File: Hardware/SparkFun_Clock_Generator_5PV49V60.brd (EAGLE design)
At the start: 27.9 x 25.4 mm, 75 parts, among them J1 QWIIC_RIGHT_ANGLE, J2 QWIIC_RIGHT_ANGLE, U1 IDT_5P49V60_CLOCK_GENERATOR, Y1 16MHz

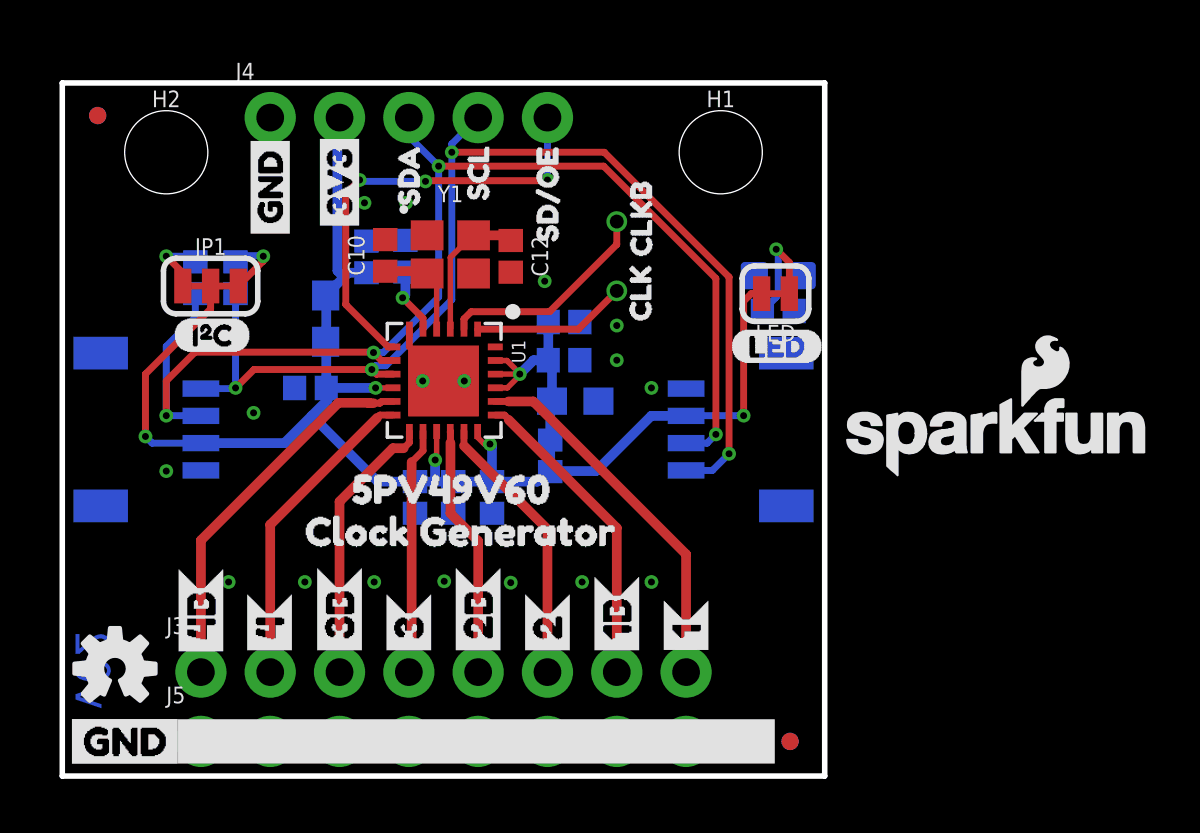
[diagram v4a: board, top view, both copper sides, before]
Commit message: Updates board with select jumper to enable select mode and fixes labels
* Also swaps clock out 4 and 4B
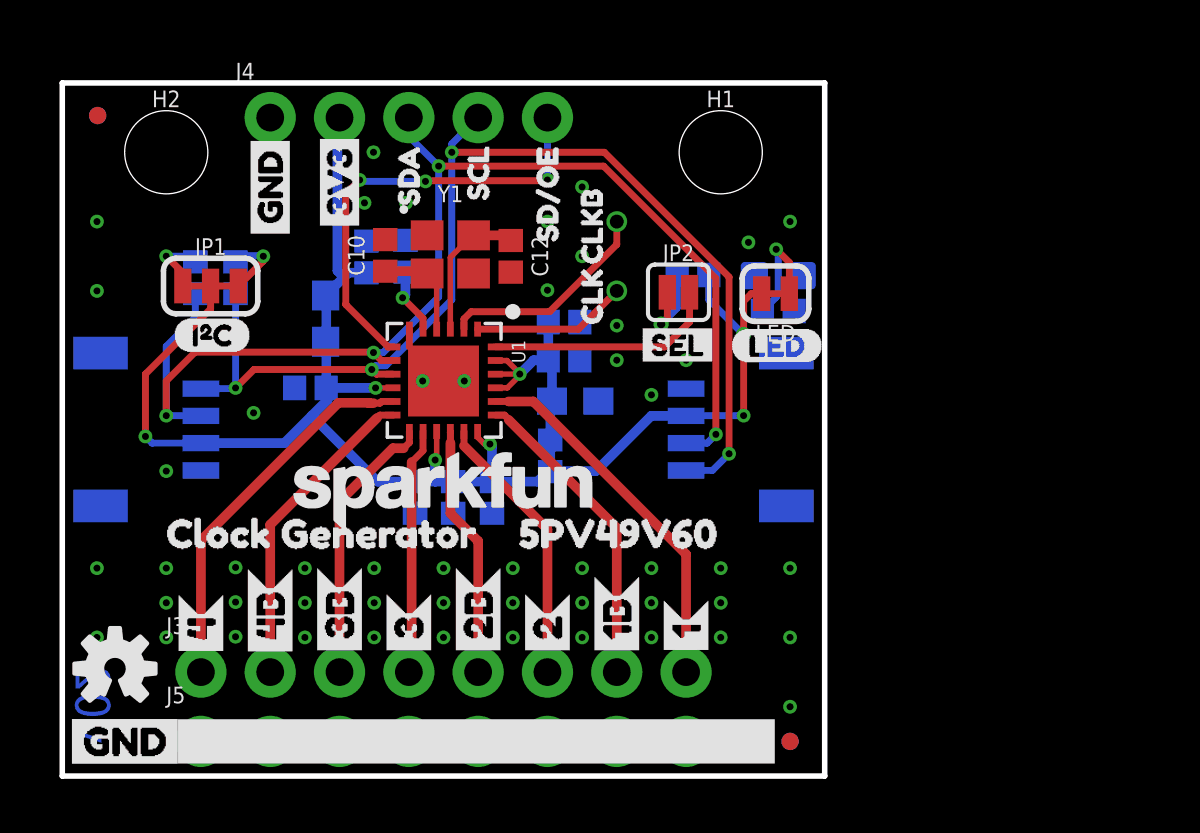
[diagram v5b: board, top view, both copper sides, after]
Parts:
- added JP2: JUMPER-SMT_2_NO_SILK, SparkFun-Jumpers:SMT-JUMPER_2_NO_SILK
- added R5: 10k, SparkFun-Resistors:0402
- added U$1: (no value), select:SEL0
- LOGO1: value SFE_LOGO_NAME_FLAME.1_INCH -> SFE_LOGO_NAME.1_INCH; device SparkFun-Aesthetics:SFE_LOGO_NAME_FLAME_.1 -> SparkFun-Aesthetics:SFE_LOGO_NAME_.1
- U$31: device Even more labels:CLKB13 -> Even more labels:CLK12
- U$32: device Even more labels:CLK11 -> Even more labels:CLKB13
- moved LOGO1 20.4 mm to (14.0, 10.4)
- moved U$31 6.38 mm to (21.4, 16.0), turned to 90 degrees
- moved U$17 6.33 mm to (15.8, 8.89)
- moved U$16 5.08 mm to (2.92, 8.89)
- moved U$4 3.48 mm to (27.8, 19.8)
- moved U$15 2.54 mm to (5.08, 9.42)
- moved U$25 2.54 mm to (7.62, 4.09)
- moved U$11 2.51 mm to (7.59, 10.4)
- moved U$38 2.51 mm to (5.08, 4.06)
- moved U$34 1.82 mm to (19.4, 18.1)
- moved U$33 1.78 mm to (19.4, 15.9)
- moved U$32 1.24 mm to (21.4, 18.3), turned to 90 degrees
- moved LOGO3 0.18 mm to (25.8, 8.38)
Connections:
- new net N$7: JP2.1, R5.2
- net 3.3V: now also R5.1
- net OUT4: now also J3.1, U1.P11; no longer J3.2, U1.P12
- net OUT4B: now also J3.2, U1.P12; no longer J3.1, U1.P11
- net SEL_I2CB: now also JP2.2
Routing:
- net SEL_I2CB: track 0.00 -> 8.59 mm
- net N$7: track 0.00 -> 3.31 mm, vias 0 -> 1
- net 3.3V: track 69.1 -> 71.8 mm, vias 7 -> 8
- net OUT4B: track 14.0 -> 11.6 mm
- net OUT4: track 11.6 -> 14.0 mm
- net GND: vias 17 -> 51

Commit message: Improves ground plane pour, adds some more vias, updates packages of clock and crystal
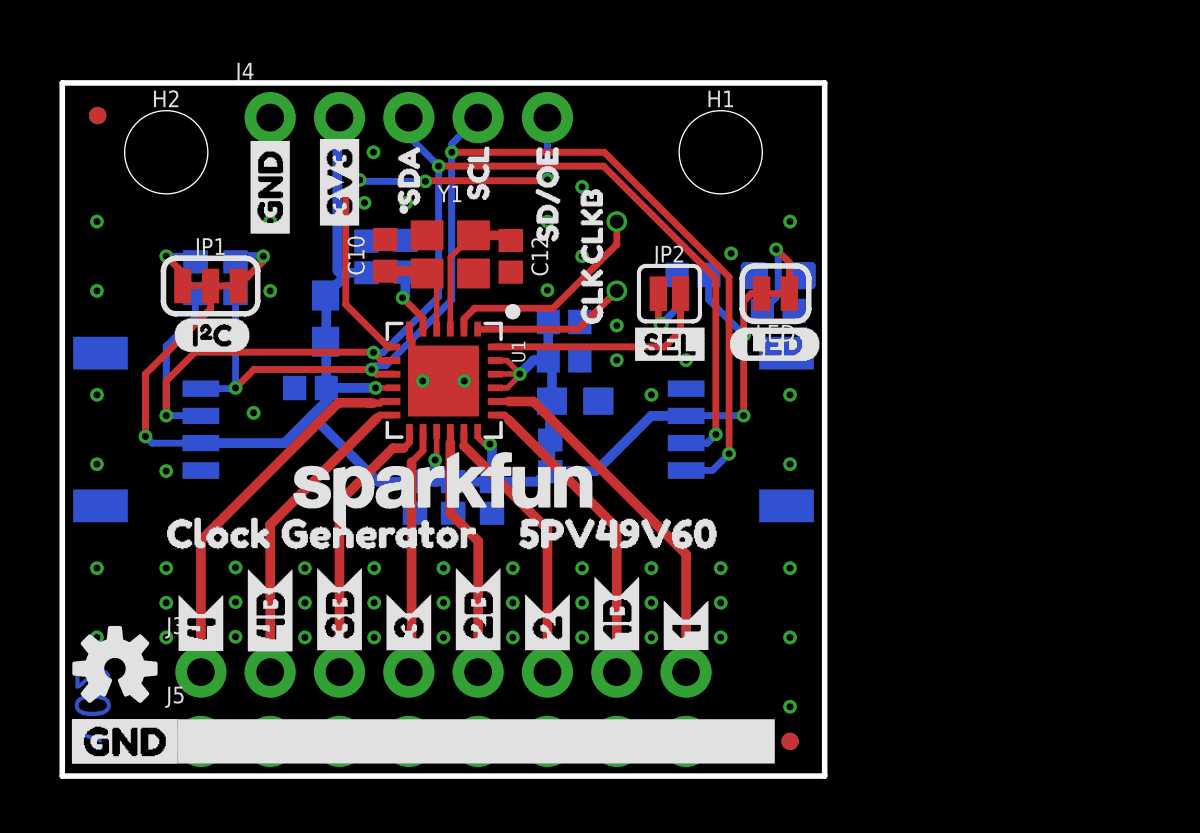
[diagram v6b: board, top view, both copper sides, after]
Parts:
- moved JP2 0.33 mm to (22.3, 17.7)
- moved U$1 0.28 mm to (20.6, 15.8)
- moved U$36 0.09 mm to (24.4, 15.8)
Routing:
- net GND: track 0.65 -> 1.00 mm, vias 51 -> 57
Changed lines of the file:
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@@
 <layer number="45" name="Holes" color="7" fill="1" visible="yes" active="yes"/>
 <layer number="46" name="Milling" color="3" fill="1" visible="no" active="yes"/>
-<layer number="47" name="Measures" color="7" fill="1" visible="yes" active="yes"/>
+<layer number="47" name="Measures" color="7" fill="1" visible="no" active="yes"/>
 <layer number="48" name="Document" color="7" fill="1" visible="no" active="yes"/>
 <layer number="49" name="Reference" color="13" fill="1" visible="yes" active="yes"/>
@@
 <element name="FD3" library="SparkFun-Aesthetics" package="FIDUCIAL-MICRO" value="FIDUCIALUFIDUCIAL" x="26.67" y="1.27" smashed="yes" rot="MR0"/>
 <element name="FD4" library="SparkFun-Aesthetics" package="FIDUCIAL-MICRO" value="FIDUCIALUFIDUCIAL" x="26.67" y="1.27" smashed="yes"/>
-<element name="JP1" library="SparkFun-Jumpers" package="SMT-JUMPER_3_2-NC_TRACE_SILK" value="JUMPER-SMT_3_2-NC_TRACE_SILK" x="5.4356" y="17.9578" smashed="yes">
+<element name="JP1" library="SparkFun-Jumpers" package="SMT-JUMPER_3_2-NC_TRACE_SILK" package3d_urn="urn:adsk.eagle:package:39289/1" value="JUMPER-SMT_3_2-NC_TRACE_SILK" x="5.4356" y="17.9578" smashed="yes">
 <attribute name="NAME" x="5.4356" y="19.1008" size="0.6096" layer="25" font="vector" ratio="20" align="bottom-center"/>
 <attribute name="VALUE" x="5.4356" y="16.8148" size="0.6096" layer="27" font="vector" ratio="20" align="top-center"/>
@@
 <attribute name="VALUE" x="26.2382" y="16.2814" size="0.6096" layer="28" font="vector" ratio="20" rot="MR0" align="top-center"/>
 </element>
-<element name="LED" library="SparkFun-Jumpers" package="SMT-JUMPER_2_NC_TRACE_SILK" value="JUMPER-SMT_2_NC_TRACE_SILK" x="26.1366" y="17.6784" smashed="yes" rot="R180">
+<element name="LED" library="SparkFun-Jumpers" package="SMT-JUMPER_2_NC_TRACE_SILK" package3d_urn="urn:adsk.eagle:package:39281/1" value="JUMPER-SMT_2_NC_TRACE_SILK" x="26.1366" y="17.6784" smashed="yes" rot="R180">
 <attribute name="NAME" x="26.1366" y="16.5354" size="0.6096" layer="25" font="vector" ratio="20" rot="R180" align="bottom-center"/>
 <attribute name="VALUE" x="26.1366" y="18.8214" size="0.6096" layer="27" font="vector" ratio="20" rot="R180" align="top-center"/>
@@
 <element name="U$34" library="Even more labels" package="CLKB13" value="" x="19.4056" y="18.0848" smashed="yes" rot="R90"/>
 <element name="U$35" library="Labels" package="I_SUPER2_C-()-03" value="" x="4.064" y="16.1544" smashed="yes"/>
-<element name="U$36" library="led" package="LED0" value="" x="24.4602" y="15.7734" smashed="yes"/>
+<element name="U$36" library="led" package="LED0" value="" x="24.384" y="15.8242" smashed="yes"/>
 <element name="J7" library="SparkFun-Connectors" package="1X01_SMALL" value="" x="20.32" y="20.32" smashed="yes"/>
 <element name="J8" library="SparkFun-Connectors" package="1X01_SMALL" value="" x="20.32" y="17.78" smashed="yes"/>
@@
 <attribute name="VALUE" x="10.414" y="16.764" size="0.6096" layer="28" font="vector" ratio="20" rot="MR270" align="top-center"/>
 </element>
-<element name="JP2" library="SparkFun-Jumpers" package="SMT-JUMPER_2_NO_SILK" package3d_urn="urn:adsk.eagle:package:39279/1" value="JUMPER-SMT_2_NO_SILK" x="22.5806" y="17.7292" smashed="yes">
-<attribute name="NAME" x="22.5806" y="18.8722" size="0.6096" layer="25" font="vector" ratio="20" align="bottom-center"/>
-<attribute name="VALUE" x="22.5806" y="16.5862" size="0.6096" layer="27" font="vector" ratio="20" align="top-center"/>
+<element name="JP2" library="SparkFun-Jumpers" package="SMT-JUMPER_2_NO_SILK" package3d_urn="urn:adsk.eagle:package:39279/1" value="JUMPER-SMT_2_NO_SILK" x="22.2504" y="17.6784" smashed="yes">
+<attribute name="NAME" x="22.2504" y="18.8214" size="0.6096" layer="25" font="vector" ratio="20" align="bottom-center"/>
+<attribute name="VALUE" x="22.2504" y="16.5354" size="0.6096" layer="27" font="vector" ratio="20" align="top-center"/>
 </element>
 <element name="R5" library="SparkFun-Resistors" package="0402" value="10k" x="23.114" y="18.3642" smashed="yes" rot="MR0">
@@
 <attribute name="VALUE" x="23.114" y="17.6022" size="0.6096" layer="28" font="vector" ratio="20" rot="MR0" align="top-center"/>
 </element>
-<element name="U$1" library="select" package="SEL0" value="" x="20.8788" y="15.7988" smashed="yes"/>
+<element name="U$1" library="select" package="SEL0" value="" x="20.5994" y="15.8242" smashed="yes"/>
 <element name="U$31" library="Even more labels" package="CLK12" value="" x="21.4122" y="16.002" smashed="yes" rot="MR90"/>
 <element name="U$32" library="Even more labels" package="CLKB13" value="" x="21.4376" y="18.288" smashed="yes" rot="MR90"/>
@@
 <via x="17.78" y="17.8054" extent="1-16" drill="0.254"/>
 <via x="7.0104" y="13.3096" extent="1-16" drill="0.254"/>
-<wire x1="12.72" y1="16.378" x2="12.72" y2="15.728" width="0.254" layer="1"/>
+<wire x1="12.8216" y1="15.9716" x2="12.72" y2="16.0732" width="0.254" layer="1"/>
+<wire x1="12.72" y1="16.378" x2="12.72" y2="16.0732" width="0.254" layer="1"/>
+<wire x1="12.8216" y1="15.9716" x2="12.8216" y2="15.4232" width="0.254" layer="1"/>
 <via x="3.81" y="11.176" extent="1-16" drill="0.254"/>
 <polygon width="0.254" layer="16" isolate="0.3048" rank="2">
@@
 <via x="19.05" y="21.59" extent="1-16" drill="0.254"/>
 <via x="22.86" y="15.24" extent="1-16" drill="0.254"/>
-<via x="25.146" y="19.558" extent="1-16" drill="0.254"/>
+<via x="24.511" y="19.1516" extent="1-16" drill="0.254"/>
+<via x="1.27" y="11.43" extent="1-16" drill="0.254"/>
+<via x="1.27" y="13.97" extent="1-16" drill="0.254"/>
+<via x="26.67" y="13.97" extent="1-16" drill="0.254"/>
+<via x="26.67" y="11.43" extent="1-16" drill="0.254"/>
+<via x="7.62" y="17.78" extent="1-16" drill="0.254"/>
+<via x="7.62" y="20.32" extent="1-16" drill="0.254"/>
 </signal>
 <signal name="3.3V">
@@
 <contactref element="J7" pad="P$1"/>
 <wire x1="14.72" y1="16.378" x2="14.72" y2="16.752" width="0.254" layer="1"/>
-<wire x1="14.72" y1="16.752" x2="14.986" y2="17.018" width="0.254" layer="1"/>
-<wire x1="14.986" y1="17.018" x2="17.8562" y2="17.018" width="0.254" layer="1"/>
+<wire x1="14.72" y1="16.752" x2="15.113" y2="17.145" width="0.254" layer="1"/>
+<wire x1="15.113" y1="17.145" x2="17.9832" y2="17.145" width="0.254" layer="1"/>
 <wire x1="20.32" y1="20.32" x2="20.32" y2="19.4818" width="0.254" layer="1"/>
-<wire x1="20.32" y1="19.4818" x2="17.8562" y2="17.018" width="0.254" layer="1"/>
+<wire x1="20.32" y1="19.4818" x2="17.9832" y2="17.145" width="0.254" layer="1"/>
 </signal>
 <signal name="N$1">
@@
 <wire x1="15.87" y1="15.728" x2="22.078" y2="15.728" width="0.254" layer="1"/>
 <contactref element="JP2" pad="2"/>
-<wire x1="22.987" y1="16.637" x2="22.987" y2="17.7292" width="0.254" layer="1"/>
-<wire x1="22.078" y1="15.728" x2="22.987" y2="16.637" width="0.254" layer="1"/>
+<wire x1="22.6568" y1="16.3068" x2="22.6568" y2="17.6784" width="0.254" layer="1"/>
+<wire x1="22.078" y1="15.728" x2="22.6568" y2="16.3068" width="0.254" layer="1"/>
 </signal>
 <signal name="N$7">
 <contactref element="R5" pad="2"/>
 <contactref element="JP2" pad="1"/>
-<wire x1="22.1742" y1="17.7292" x2="22.1742" y2="16.7894" width="0.254" layer="1"/>
-<wire x1="22.1742" y1="16.7894" x2="21.9456" y2="16.5608" width="0.254" layer="1"/>
+<wire x1="21.844" y1="17.6784" x2="21.844" y2="16.6624" width="0.254" layer="1"/>
+<wire x1="21.844" y1="16.6624" x2="21.9456" y2="16.5608" width="0.254" layer="1"/>
 <via x="21.9456" y="16.5608" extent="1-16" drill="0.3048"/>
 <wire x1="22.534" y1="18.3642" x2="22.534" y2="17.1492" width="0.254" layer="16"/>

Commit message: Checks DRC and fixes errors
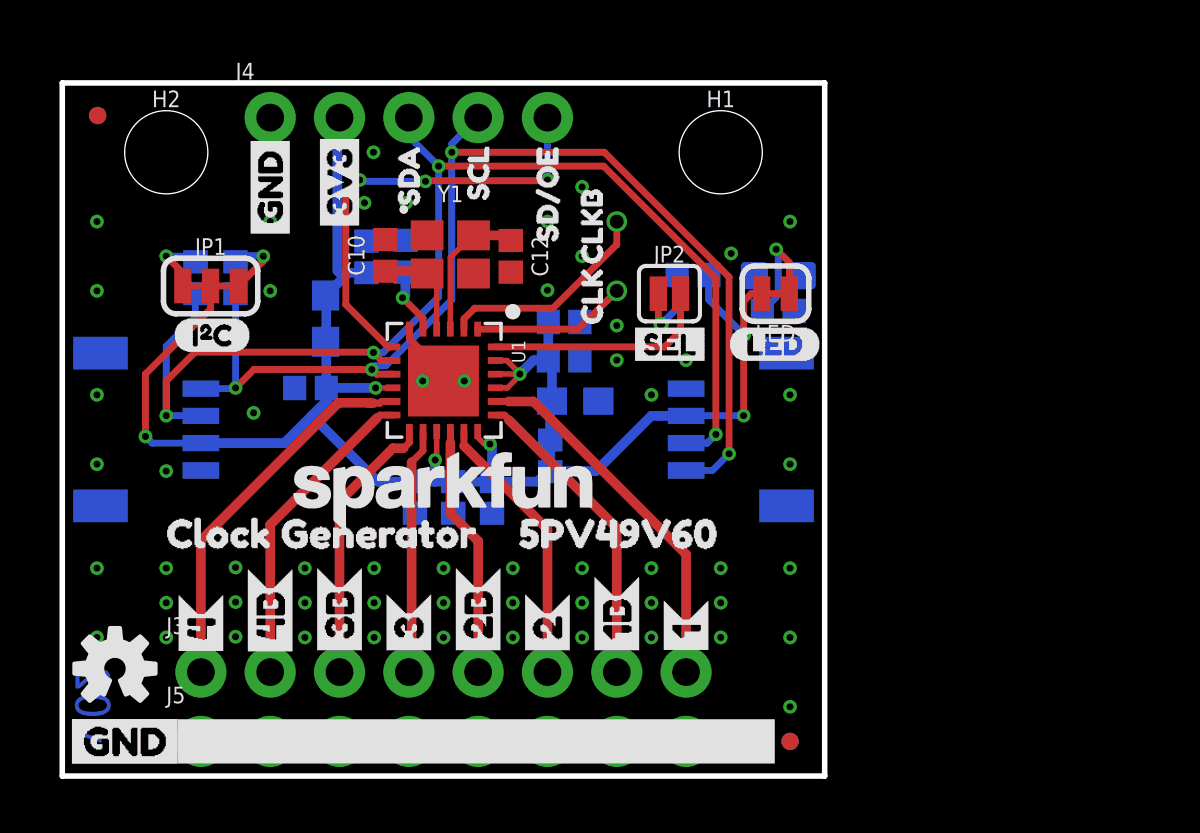
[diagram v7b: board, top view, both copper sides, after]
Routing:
- net GND: track 1.00 -> 2.42 mm
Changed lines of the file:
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@@
 <via x="17.78" y="17.8054" extent="1-16" drill="0.254"/>
 <via x="7.0104" y="13.3096" extent="1-16" drill="0.254"/>
-<wire x1="12.8216" y1="15.9716" x2="12.72" y2="16.0732" width="0.254" layer="1"/>
-<wire x1="12.72" y1="16.378" x2="12.72" y2="16.0732" width="0.254" layer="1"/>
-<wire x1="12.8216" y1="15.9716" x2="12.8216" y2="15.4232" width="0.254" layer="1"/>
 <via x="3.81" y="11.176" extent="1-16" drill="0.254"/>
 <polygon width="0.254" layer="16" isolate="0.3048" rank="2">
@@
 <via x="7.62" y="17.78" extent="1-16" drill="0.254"/>
 <via x="7.62" y="20.32" extent="1-16" drill="0.254"/>
+<wire x1="12.72" y1="16.0328" x2="12.72" y2="16.378" width="0.254" layer="1"/>
+<wire x1="13.97" y1="14.478" x2="13.97" y2="14.7828" width="0.254" layer="1"/>
+<wire x1="13.97" y1="14.7828" x2="12.72" y2="16.0328" width="0.254" layer="1"/>
 </signal>
 <signal name="3.3V">
@@
 <wire x1="3.048" y1="12.446" x2="3.294" y2="12.2" width="0.254" layer="16"/>
 <wire x1="3.294" y1="12.2" x2="5.08" y2="12.2" width="0.254" layer="16"/>
-<wire x1="11.4808" y1="14.224" x2="11.4554" y2="14.1986" width="0.3556" layer="16"/>
 <wire x1="13.72" y1="11.6372" x2="13.6652" y2="11.5824" width="0.2032" layer="1"/>
 <wire x1="13.72" y1="12.628" x2="13.72" y2="11.6372" width="0.2032" layer="1"/>

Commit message: Fixes "SEL" text, adds second ground pour for clock lines isolate only, fixes power shorting through ferrite and resistor
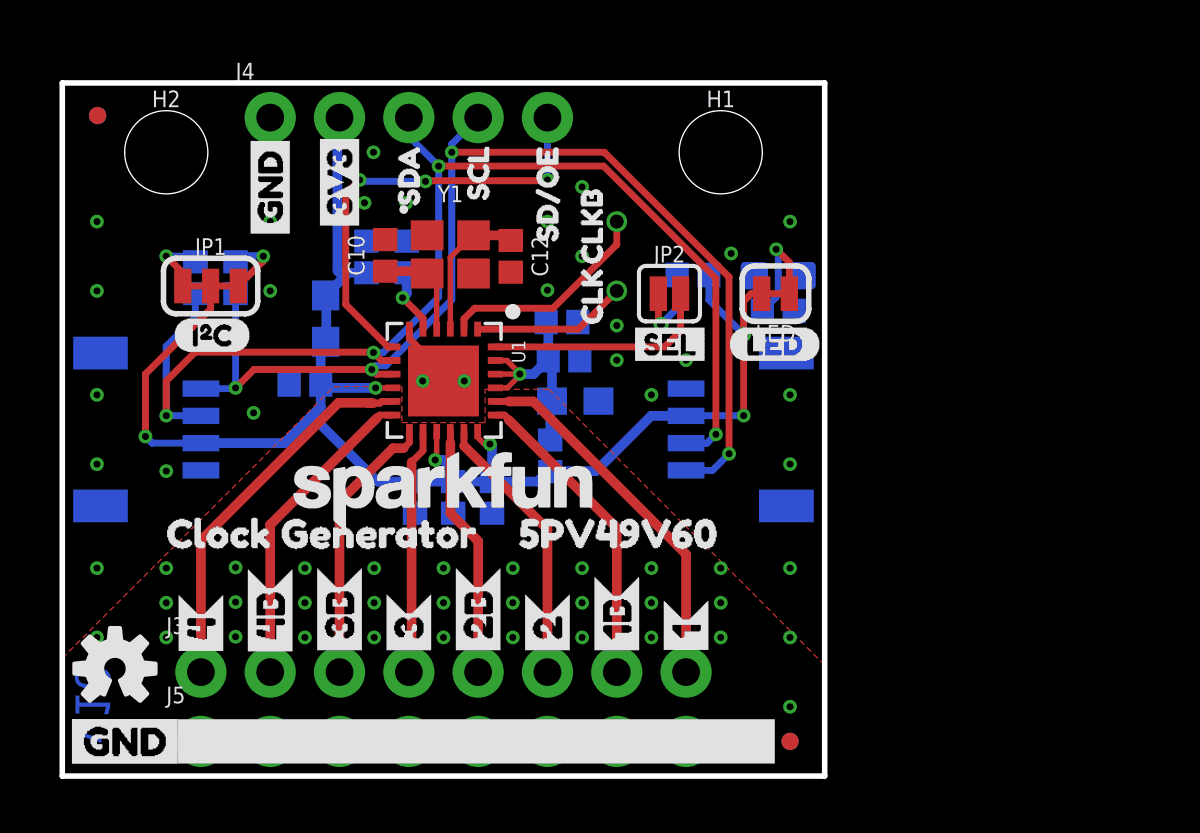
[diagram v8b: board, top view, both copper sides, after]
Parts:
- U$10: device Bottom Clock Labels:CLK3B5 -> Top clock labels:3B5
- U$11: device Bottom Clock Labels:CLK4B7 -> Top clock labels:34
- U$12: device Bottom Clock Labels:CLK10 -> Top clock labels:2B3
- U$13: device Bottom Clock Labels:CLK22 -> Top clock labels:22
- U$14: device Bottom Clock Labels:CLK34 -> Top clock labels:1B1
- U$15: device Bottom Clock Labels:CLK46 -> Top clock labels:10
- U$8: device Bottom Clock Labels:CLK1B1 -> Top clock labels:46
- U$9: device Bottom Clock Labels:CLK2B3 -> Top clock labels:4B7
- moved U$15 18.5 mm to (22.9, 4.14), turned to 90 degrees
- moved U$8 16.4 mm to (5.08, 4.06), turned to 90 degrees
- moved U$9 9.90 mm to (7.62, 4.09), turned to 90 degrees
- moved U$14 9.37 mm to (20.3, 4.09), turned to 90 degrees
- moved U$12 9.19 mm to (15.2, 4.09), turned to 90 degrees
- moved U$11 8.13 mm to (12.7, 4.09), turned to 90 degrees
- moved U$10 6.32 mm to (10.2, 4.09), turned to 90 degrees
- moved C2 5.97 mm to (8.89, 14.4), turned to 0 degrees
- moved C7 5.96 mm to (12.6, 19.0), turned to 90 degrees
- moved U$13 5.44 mm to (17.8, 4.09), turned to 90 degrees
- moved C1 0.08 mm to (18.3, 16.6)
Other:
- board text added: "v10"
- board text removed: "v02"
